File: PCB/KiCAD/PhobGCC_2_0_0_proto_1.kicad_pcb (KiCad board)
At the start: 2 copper layers, 125.5 x 90.3 mm, 113 parts, among them J1 Conn_01x06_Female, J11 Conn_01x02, J14 Conn_01x06, J15 Conn_01x06, J2 Conn_01x02, J3 Conn_01x02, J4 Conn_01x01, J5 Rumble, J6 Conn_01x06, J8 USB_B_Micro, Q1 Q_NMOS_GSD, Q2 Q_PMOS_GDS, Q3 Q_NMOS_GSD, SW1 A, SW10 Dup, SW11 Dright, SW12 Ddown, SW2 B, SW3 X, SW4 Y, SW5 Start, SW6 L, SW7 R, SW8 Z, SW9 Dleft, U1 MCP3202, U10 DRV5055A3xDBZxQ1, U11 DRV5055A3xDBZxQ1, U12 USBLC6-2P6, U13 USBLC6-2P6, U2 Stickbox_Assembly_Main, U3 MCP3202, U4 DRV5055A3xDBZxQ1, U5 Stickbox_Assembly_CStick, U6 AMS1117-3.3, U7 W25Q128JVS, U8 RP2040, U9 DRV5055A3xDBZxQ1, Y1 Crystal_GND24

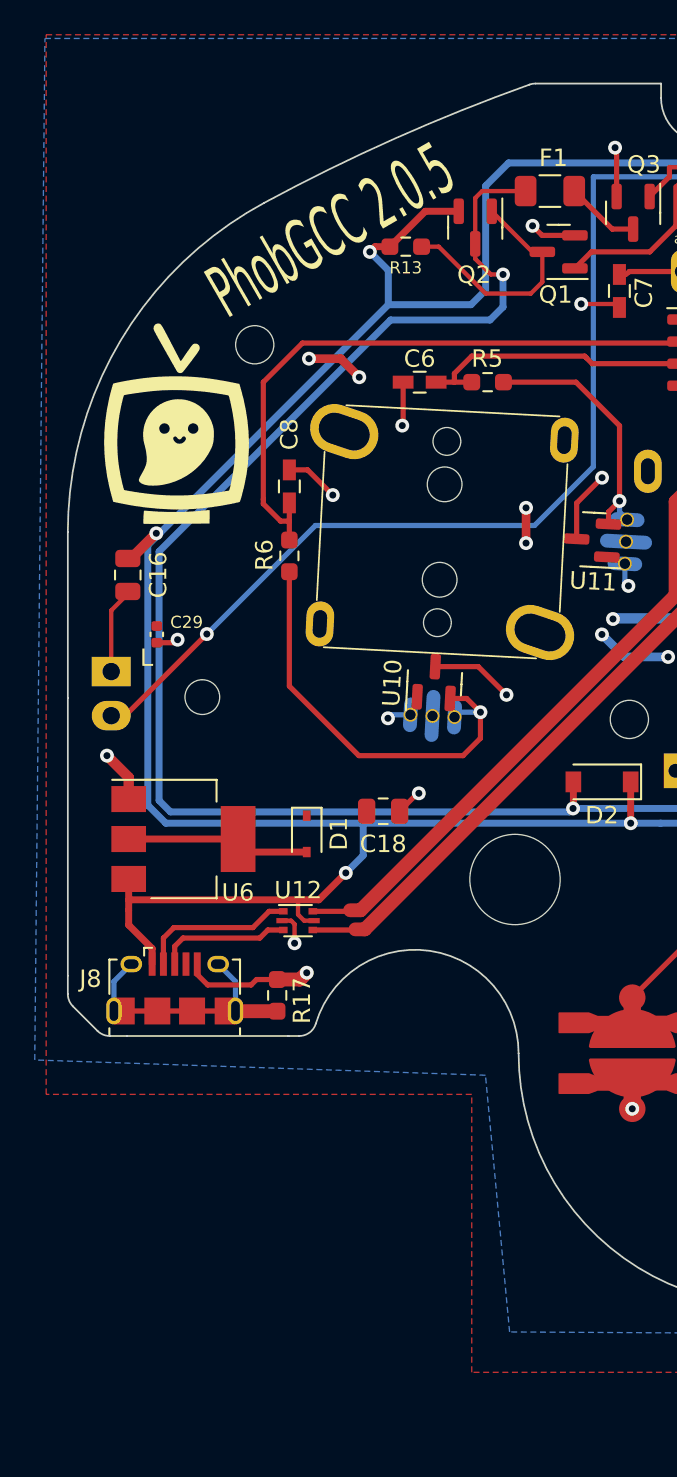
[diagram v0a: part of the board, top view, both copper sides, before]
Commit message: Implemented USB-C For Flashing
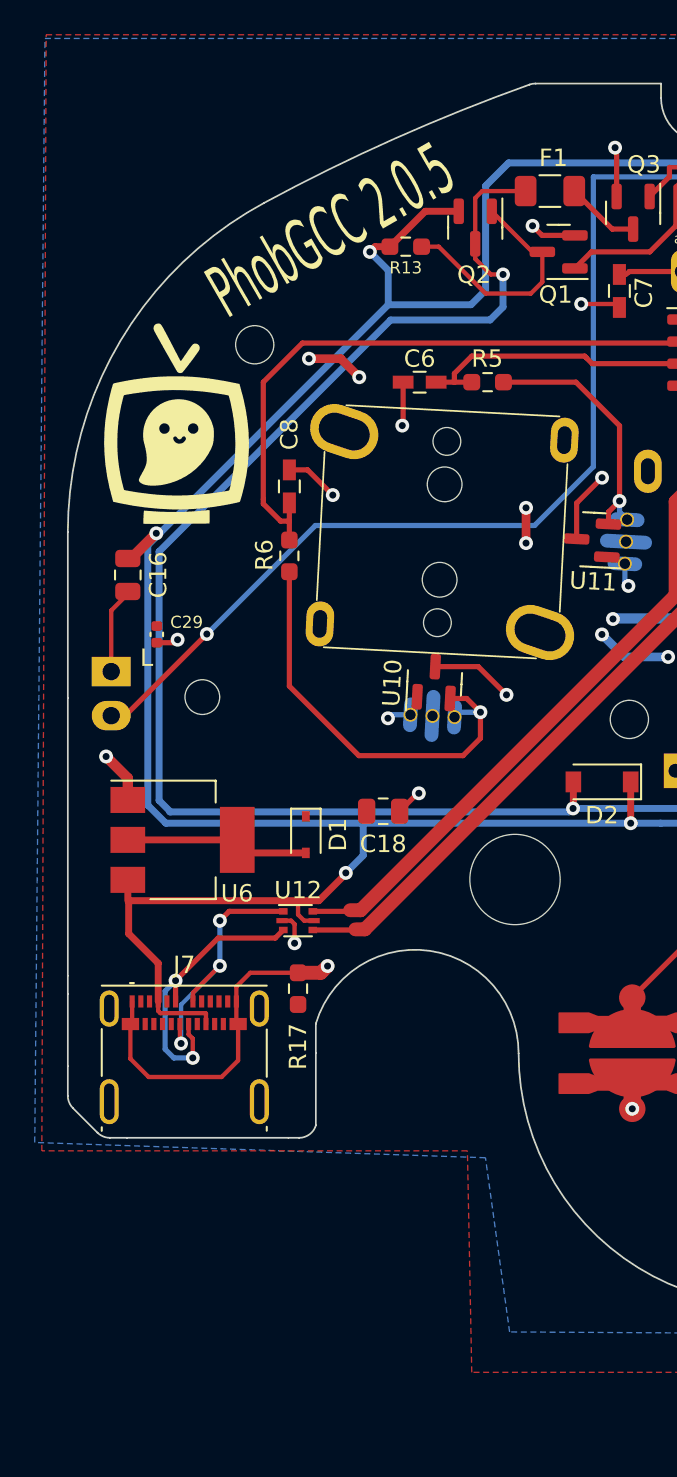
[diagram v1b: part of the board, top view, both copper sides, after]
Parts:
- removed J8: USB_B_Micro, PhobGCC_2_0_0_footprints:USB_Micro-B_Amphenol_10118194_Horizontal
- added J7: USB-C, Connector_USB:USB_C_Receptacle_Molex_105450-0101, F.Cu at (55.0, 81.4)
- moved R17 1.26 mm to (61.5, 77.4)
- moved D1 0.07 mm to (62.0, 68.5)
- moved U6 0.07 mm to (54.9, 68.8)
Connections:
- R17 pad 1: Net-(J8-Pad6) -> unconnected-(R17-Pad1)
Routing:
- net Net-(J8-Pad6): track 14.4 -> 0.00 mm
- net GND: track 140.9 -> 153.9 mm
- net /USB_D+_Raw: track 7.66 -> 16.7 mm, vias 0 -> 2
- net /USB_D-_Raw: track 9.04 -> 15.7 mm, vias 0 -> 3
- net +5V: track 159.0 -> 165.2 mm
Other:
- outline, holes or cut-outs redrawn
